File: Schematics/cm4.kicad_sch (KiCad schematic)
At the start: 50 parts, among them J1 ETHERNET, J10 RPI FAN, J11 RPI GPIO, J2 MICRO SD CARD, J3 HDMI, J4 CAMERA, J5 DISPLAY, J6 MICRO USB, J7 USB_A, J8 USB JST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

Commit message: Update Schematics
Update CM4, X42, XYmatics-E64 schematics
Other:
- company: (none) -> XYmatics E64
- title: RPI-CM4 -> XYmatics E64
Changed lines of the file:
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@@
 	(paper "User" 457.2 279.4)
 	(title_block
-		(title "RPI-CM4")
-		(date "2025-07-07")
+		(title "XYmatics E64")
+		(date "2025-07-20")
+		(rev "0.0")
+		(company "XYmatics E64")
 	)
 	(junction

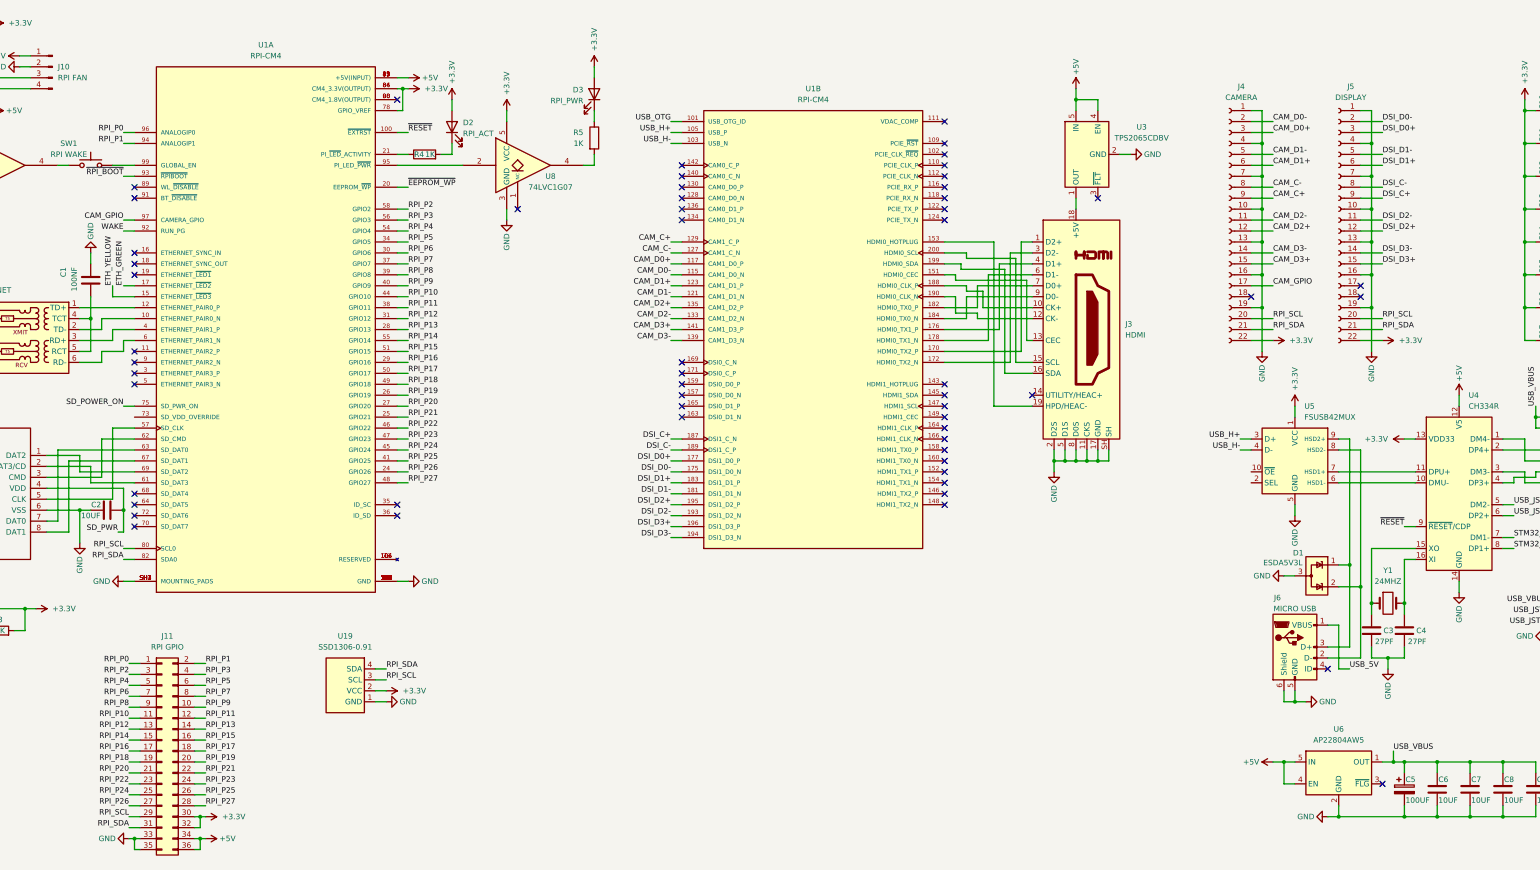
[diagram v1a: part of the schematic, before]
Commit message: Update X42 schematics, Add project PCB
Removed Neopixel and BLTouch breakouts from X42, added X42 PCB (unfinished)
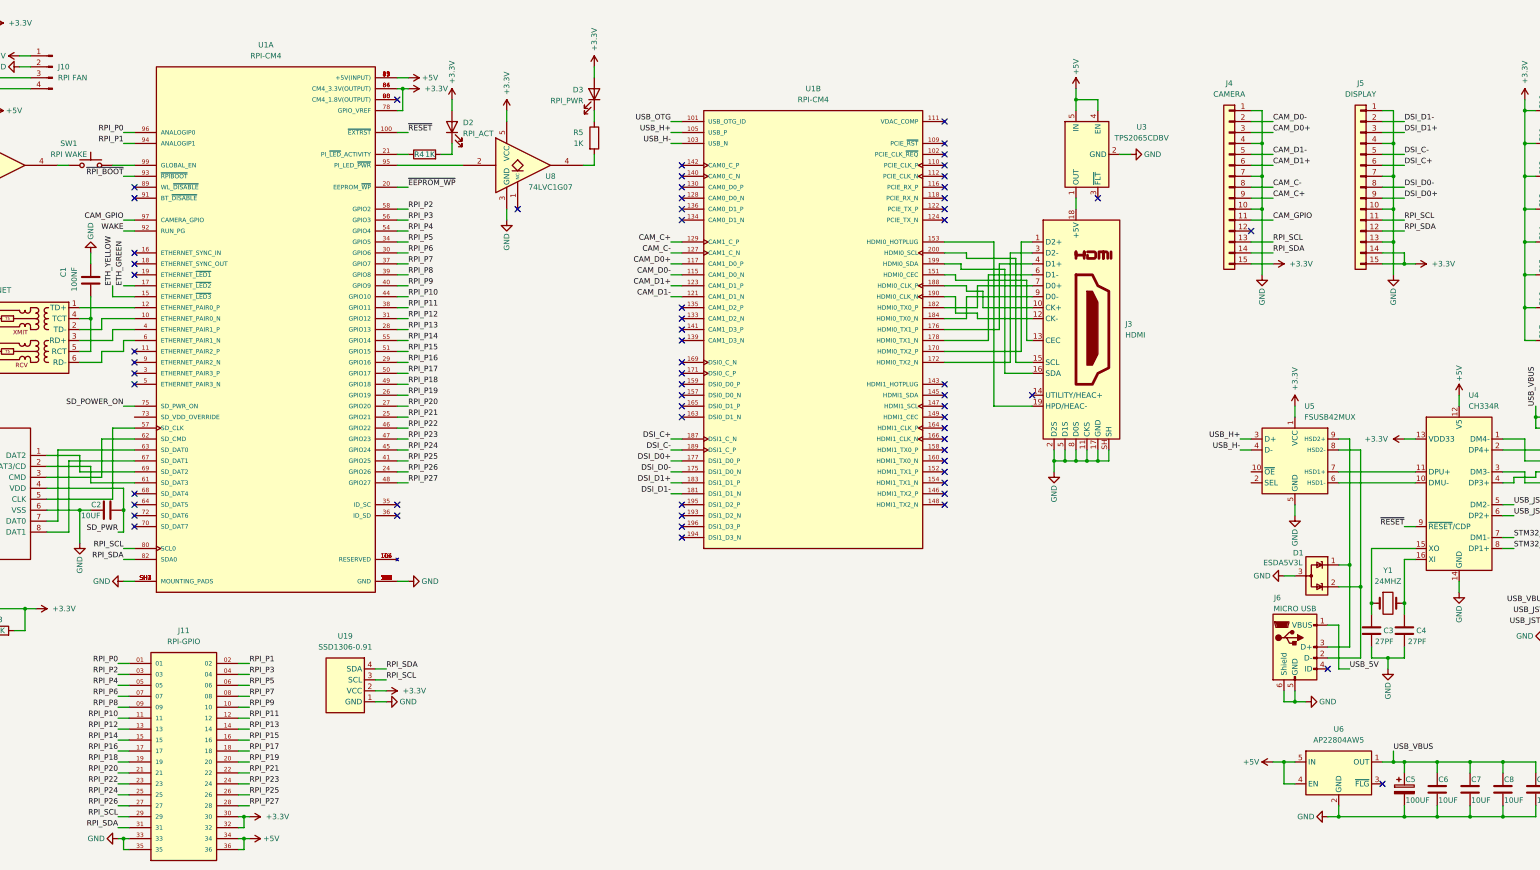
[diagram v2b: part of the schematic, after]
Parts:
- removed J11: RPI GPIO, symbol Connector_Generic:Conn_02x18_Odd_Even
- removed J4: CAMERA, symbol Connector:Conn_01x22_Socket
- removed J5: DISPLAY, symbol Connector:Conn_01x22_Socket
- added J11: RPI-GPIO, TST-118-01-T-D:SAMTEC_TST-118-01-T-D, symbol TST-118-01-T-D:TST-118-01-T-D
- added J4: CAMERA, Connector_FFC-FPC:Molex_502231-1500_1x15-1SH_P0.5mm_Vertical, symbol Connector_Generic:Conn_01x15
- added J5: DISPLAY, Connector_FFC-FPC:Molex_502231-1500_1x15-1SH_P0.5mm_Vertical, symbol Connector_Generic:Conn_01x15
- C1, C10, C11, C12, C13, C14, C15, C16, C17, C18, C2, C3, C4, C6, C7, C8, C9: footprint (none) -> Capacitor_SMD:C_0805_2012Metric
- C5: footprint (none) -> Capacitor_SMD:CP_Elec_5x3
- D2, D3: footprint (none) -> LED_SMD:LED_0805_2012Metric
- J2: footprint (none) -> Connector_Card:microSD_HC_Wuerth_693072010801
- J3: footprint (none) -> Connector_Video:HDMI_A_Molex_208658-1001_Horizontal
- J6: footprint (none) -> Connector_USB:USB_Micro-B_Molex_47346-0001
- J7: footprint (none) -> Connector_USB:USB_A_CUI_UJ2-ADH-TH_Horizontal_Stacked
- R1, R2, R3, R4, R5, R6: footprint (none) -> Resistor_SMD:R_0805_2012Metric
- SW1: footprint (none) -> Button_Switch_SMD:SW_Tactile_SPST_NO_Straight_CK_PTS636Sx25SMTRLFS
- U7, U8: footprint (none) -> Package_TO_SOT_SMD:SOT-23-5
- Y1: footprint (none) -> Crystal:Crystal_HC49-4H_Vertical
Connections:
- net +3.3V: now also J11.30, J11.32, J4.15 (Pin_15), J5.14 (Pin_14), J5.15 (Pin_15)
- net +5V: now also J11.34, J11.36
- net CAM_C+: now also J4.9 (Pin_9)
- net CAM_C-: now also J4.8 (Pin_8)
- net CAM_D0+: now also J4.3 (Pin_3)
- net CAM_D0-: now also J4.2 (Pin_2)
- net CAM_D1+: now also J4.6 (Pin_6)
- net CAM_D1-: now also J4.5 (Pin_5)
- net CAM_GPIO: now also J4.11 (Pin_11)
- net DSI_C+: now also J5.6 (Pin_6)
- net DSI_C-: now also J5.5 (Pin_5)
- net DSI_D0+: now also J5.9 (Pin_9)
- net DSI_D0-: now also J5.8 (Pin_8)
- net DSI_D1+: now also J5.3 (Pin_3)
- net DSI_D1-: now also J5.2 (Pin_2)
- net GND: now also J11.33, J11.35, J4.1 (Pin_1), J4.10 (Pin_10), J4.4 (Pin_4), J4.7 (Pin_7), J5.1 (Pin_1), J5.10 (Pin_10), J5.13 (Pin_13), J5.4 (Pin_4), J5.7 (Pin_7)
- net RPI_P0: now also J11.01
- net RPI_P1: now also J11.02
- net RPI_P10: now also J11.11
- net RPI_P11: now also J11.12
- net RPI_P12: now also J11.13
- net RPI_P13: now also J11.14
- net RPI_P14: now also J11.15
- net RPI_P15: now also J11.16
- net RPI_P16: now also J11.17
- net RPI_P17: now also J11.18
- net RPI_P18: now also J11.19
- net RPI_P19: now also J11.20
- net RPI_P2: now also J11.03
- net RPI_P20: now also J11.21
- net RPI_P21: now also J11.22
- net RPI_P22: now also J11.23
- net RPI_P23: now also J11.24
- net RPI_P24: now also J11.25
- net RPI_P25: now also J11.26
- net RPI_P26: now also J11.27
- net RPI_P27: now also J11.28
- net RPI_P3: now also J11.04
- net RPI_P4: now also J11.05
- net RPI_P5: now also J11.06
- net RPI_P6: now also J11.07
- net RPI_P7: now also J11.08
- net RPI_P8: now also J11.09
- net RPI_P9: now also J11.10
- net RPI_SCL: now also J11.29, J4.13 (Pin_13), J5.11 (Pin_11)
- net RPI_SDA: now also J11.31, J4.14 (Pin_14), J5.12 (Pin_12)
- net CAM_D2+: no longer names the net of U1.135 (CAM1_D2_P)
- net CAM_D2-: no longer names the net of U1.133 (CAM1_D2_N)
- net CAM_D3+: no longer names the net of U1.141 (CAM1_D3_P)
- net CAM_D3-: no longer names the net of U1.139 (CAM1_D3_N)
- net DSI_D2+: no longer names the net of U1.195 (DSI1_D2_P)
- net DSI_D2-: no longer names the net of U1.193 (DSI1_D2_N)
- net DSI_D3+: no longer names the net of U1.196 (DSI1_D3_P)
- net DSI_D3-: no longer names the net of U1.194 (DSI1_D3_N)
- no-connect marks 61 -> 67

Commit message: Update E64 schematics
Finish E64 PCB
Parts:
- removed Y1: 24MHZ, Crystal:Crystal_HC49-4H_Vertical, symbol Device:Crystal
- added Y4: 24MHZ, Crystal:Crystal_SMD_Abracon_ABM3B-4Pin_5.0x3.2mm, symbol Device:Crystal_GND24
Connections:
- net GND: now also Y4.2, Y4.4
- net at C3.1, U4.15 (XO): now also Y4.1
- net at C4.1, U4.16 (XI): now also Y4.3
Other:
- moved on the sheet: J7
